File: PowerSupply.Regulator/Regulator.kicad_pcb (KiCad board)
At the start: 2 copper layers, 25 parts, among them P1 PWR_IN_2P, P2 PWR_OUT_4P, U1 SP34063A, U2 SPX29152

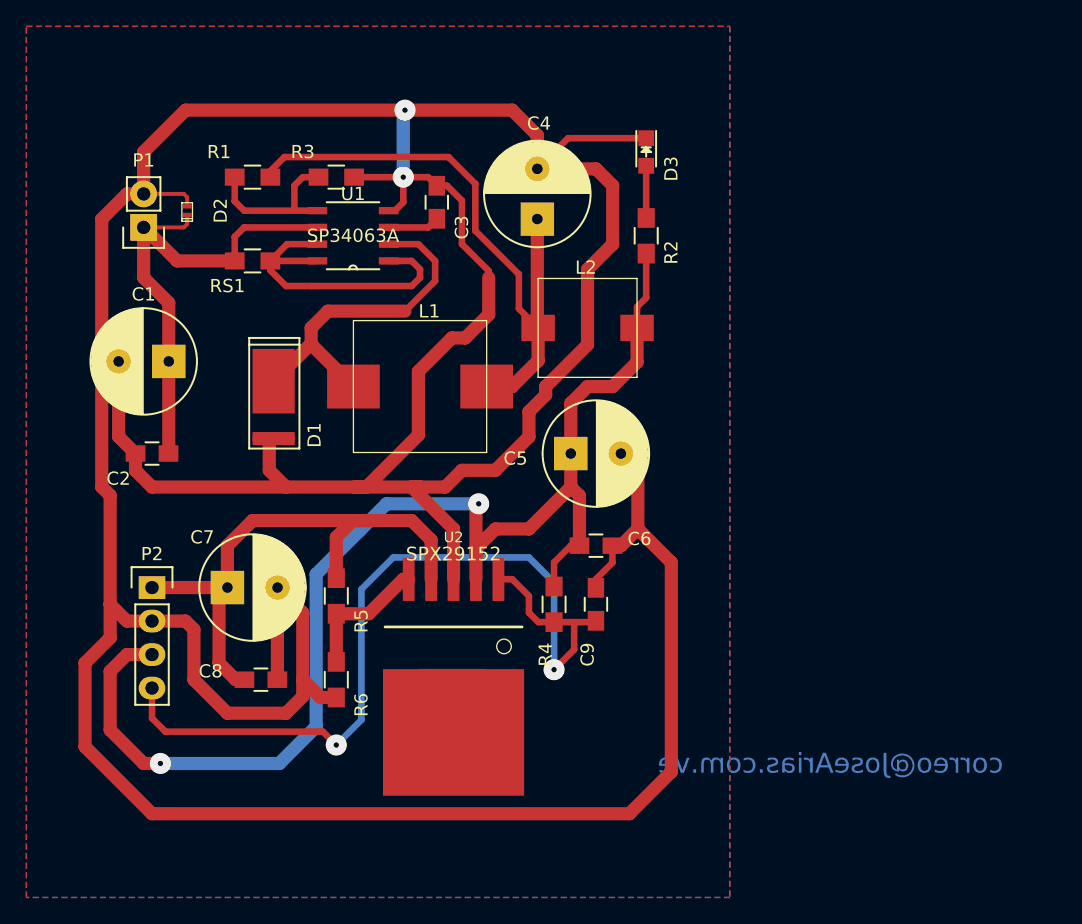
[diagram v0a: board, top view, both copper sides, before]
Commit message: Revision de PCbs + generacion de nuevos archivos Gerber
  - Se corrigen pads de pin headers
  - Se revisan
  - MainBoard option 2
  - PortExpander MC33996.Option3
  - GpibPortExpanderPCA6408A.Option3
  - Se generan Gerber + Vistas 3D
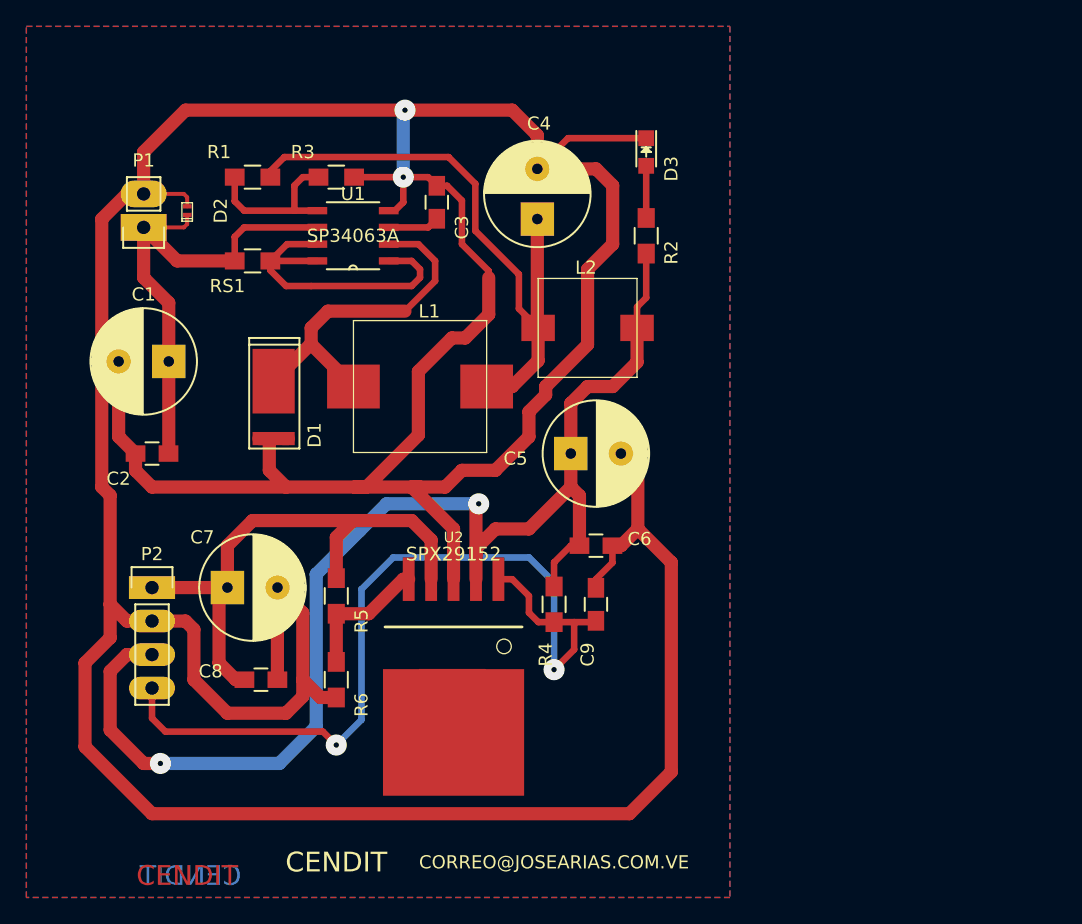
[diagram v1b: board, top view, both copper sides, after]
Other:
- board text added: "CENDIT"
- board text added: "CORREO@JOSEARIAS.COM.VE"
- board text removed: "correo@JoseArias.com.ve"
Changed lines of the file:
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@@
-(kicad_pcb (version 4) (host pcbnew 4.0.6)
+(kicad_pcb (version 4) (host pcbnew 4.0.6-e0-6349~53~ubuntu14.04.1)
   (general
     (links 50)
     (no_connects 0)
-    (area 0 0 0 0)
+    (area 111.8 63.54 170.14 134.58)
     (thickness 1.6)
-    (drawings 3)
+    (drawings 8)
     (tracks 231)
     (zones 0)
@@
   (layers
     (0 F.Cu signal)
-    (31 B.Cu signal hide)
+    (31 B.Cu signal)
     (32 B.Adhes user)
     (33 F.Adhes user)
@@
   )
   (setup
-    (last_trace_width 1)
+    (last_trace_width 0.25)
     (user_trace_width 0.3)
     (user_trace_width 0.5)
@@
     (mod_text_size 1 1)
     (mod_text_width 0.15)
-    (pad_size 5 3)
-    (pad_drill 0)
+    (pad_size 3.5 1.7272)
+    (pad_drill 1.016)
     (pad_to_mask_clearance 0)
     (aux_axis_origin 0 0)
@@
       (effects (font (size 1 1) (thickness 0.15)))
     )
-    (fp_text value PWR_IN_2P (at 2.54 0.635 270) (layer F.Fab)
+    (fp_text value PWR_IN_2P (at 2.794 1.143 270) (layer F.Fab)
       (effects (font (size 1 1) (thickness 0.15)))
     )
@@
     (fp_line (start -1.27 1.27) (end -1.27 3.81) (layer F.SilkS) (width 0.15))
     (fp_line (start -1.27 3.81) (end 1.27 3.81) (layer F.SilkS) (width 0.15))
-    (pad 1 thru_hole rect (at 0 0 180) (size 2.032 2.032) (drill 1.016) (layers *.Cu *.Mask)
+    (pad 1 thru_hole rect (at 0 0 180) (size 3.5 2.032) (drill 1.016) (layers *.Cu *.Mask)
       (net 10 VIN))
-    (pad 2 thru_hole oval (at 0 2.54 180) (size 2.032 2.032) (drill 1.016) (layers *.Cu *.Mask)
+    (pad 2 thru_hole oval (at 0 2.54 180) (size 3.5 2.032) (drill 1.016) (layers *.Cu *.Mask)
       (net 1 GNDPWR))
     (model Pin_Headers.3dshapes/Pin_Header_Straight_1x02.wrl
@@
     (fp_line (start -1.55 0) (end -1.55 -1.55) (layer F.SilkS) (width 0.15))
     (fp_line (start -1.55 -1.55) (end 1.55 -1.55) (layer F.SilkS) (width 0.15))
-    (pad 1 thru_hole rect (at 0 0) (size 2.032 1.7272) (drill 1.016) (layers *.Cu *.Mask)
+    (pad 1 thru_hole rect (at 0 0) (size 3.5 1.7272) (drill 1.016) (layers *.Cu *.Mask)
       (net 12 VOUT))
-    (pad 2 thru_hole oval (at 0 2.54) (size 2.032 1.7272) (drill 1.016) (layers *.Cu *.Mask)
-      (net 1 GNDPWR))
-    (pad 3 thru_hole oval (at 0 5.08) (size 2.032 1.7272) (drill 1.016) (layers *.Cu *.Mask)
+    (pad 2 thru_hole oval (at 0 2.54) (size 3.5 1.7272) (drill 1.016) (layers *.Cu *.Mask)
+      (net 1 GNDPWR))
+    (pad 3 thru_hole oval (at 0 5.08) (size 3.5 1.7272) (drill 1.016) (layers *.Cu *.Mask)
       (net 11 VREG))
-    (pad 4 thru_hole oval (at 0 7.62) (size 2.032 1.7272) (drill 1.016) (layers *.Cu *.Mask)
+    (pad 4 thru_hole oval (at 0 7.62) (size 3.5 1.7272) (drill 1.016) (layers *.Cu *.Mask)
       (net 2 /ENABLE))
     (model Pin_Headers.3dshapes/Pin_Header_Straight_1x04.wrl
@@
       (net 6 "Net-(C4-Pad1)"))
   )
-  (gr_text correo@JoseArias.com.ve (at 175.26 121.92) (layer B.Cu)
+  (gr_text CENDIT (at 126.746 130.429) (layer B.Cu)
     (effects (font (size 1.5 1.5) (thickness 0.3)) (justify mirror))
   )
+  (gr_text CORREO@JOSEARIAS.COM.VE (at 154.432 129.413) (layer B.SilkS)
+    (effects (font (size 1 1) (thickness 0.25)) (justify mirror))
+  )
+  (gr_text CORREO@JOSEARIAS.COM.VE (at 154.305 129.413) (layer F.SilkS)
+    (effects (font (size 1 1) (thickness 0.25)))
+  )
+  (gr_text CENDIT (at 138.049 129.413) (layer B.SilkS)
+    (effects (font (size 1.5 1.5) (thickness 0.3)) (justify mirror))
+  )
+  (gr_text CENDIT (at 137.795 129.413) (layer F.SilkS)
+    (effects (font (size 1.5 1.5) (thickness 0.3)))
+  )
+  (gr_text CENDIT (at 126.492 130.429) (layer F.Cu)
+    (effects (font (size 1.5 1.5) (thickness 0.3)))
+  )
   (target plus (at 167.64 66.04) (size 5) (width 0.1) (layer Edge.Cuts))

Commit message: Revision de PCBs + generacion nuevos gerber
  - Se hacen ligeras correcciones en los PCBs (5)
  - Se genera nuevamente archivo PCBs combinados
  - Se generan nuevos archivos gerber
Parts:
- moved R4 2.36 mm to (156.2, 111.3)
- moved C9 2.26 mm to (159.3, 111.3)
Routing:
- net /ENABLE: track 66.5 -> 76.2 mm
- net Net-(C4-Pad1): track 46.4 -> 41.4 mm
- net Net-(D1-Pad1): track 26.2 -> 30.1 mm
- net GNDPWR: track 346.7 -> 343.6 mm
